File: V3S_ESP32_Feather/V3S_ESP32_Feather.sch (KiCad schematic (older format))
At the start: 10 parts, among them J1 USB_B_Micro, J10 UART, J2 Bat, J4 PWM, J8 I2C

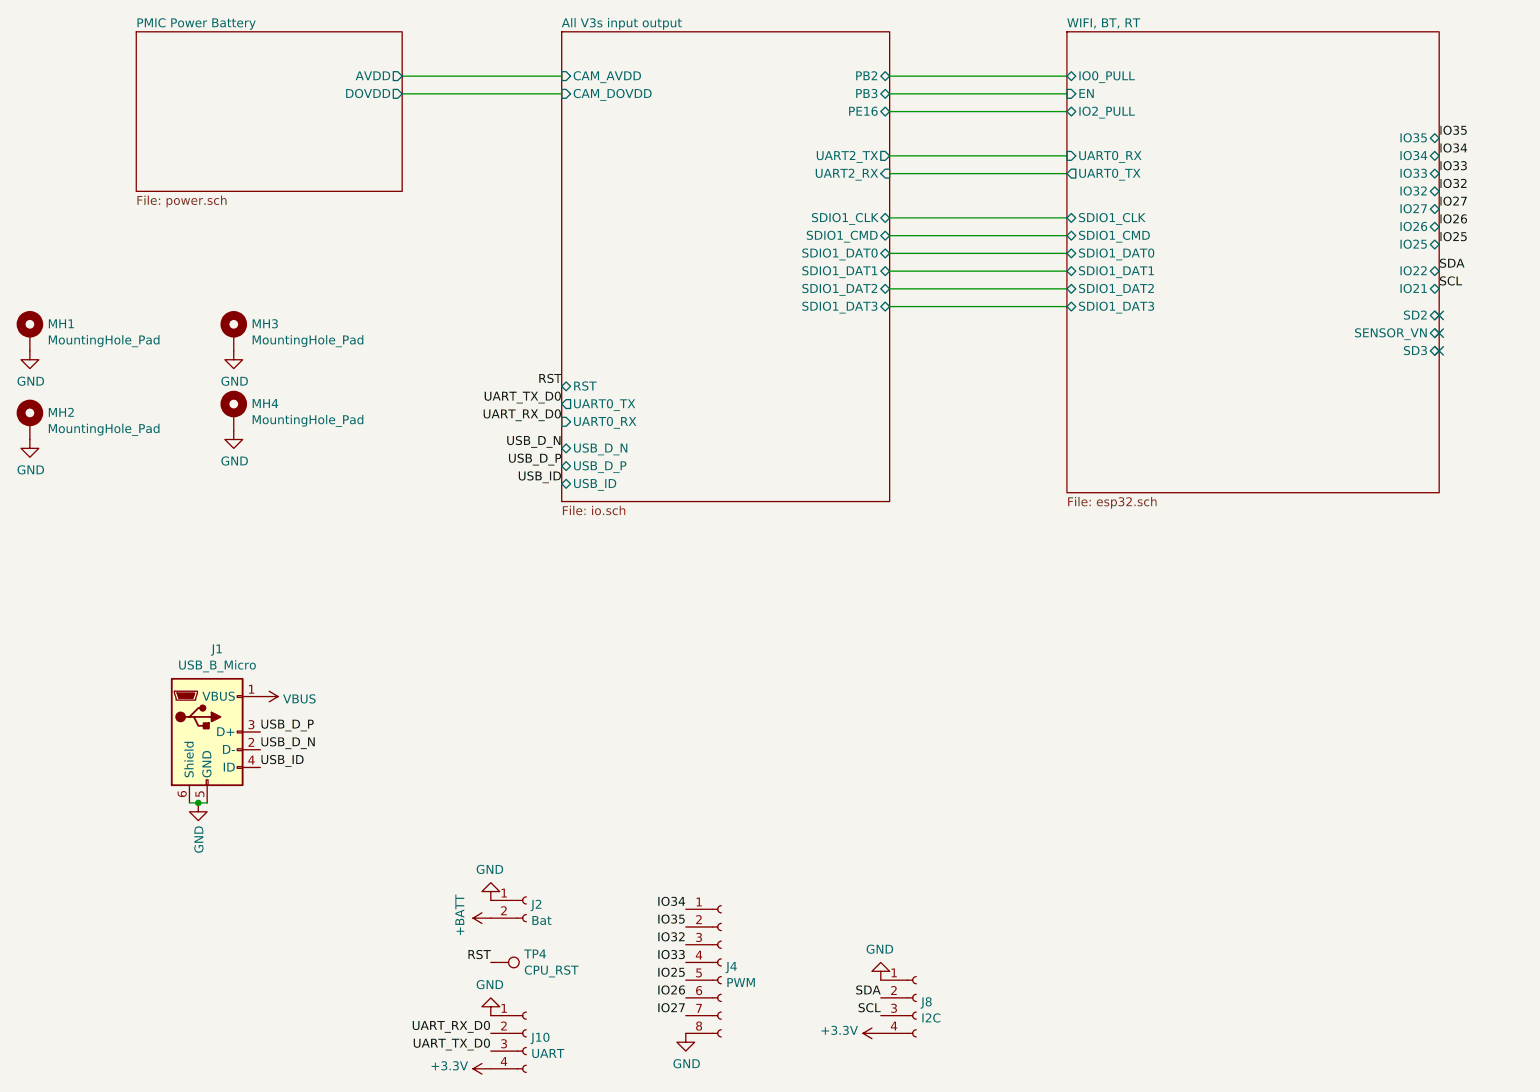
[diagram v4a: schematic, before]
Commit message: Sdcard part routed
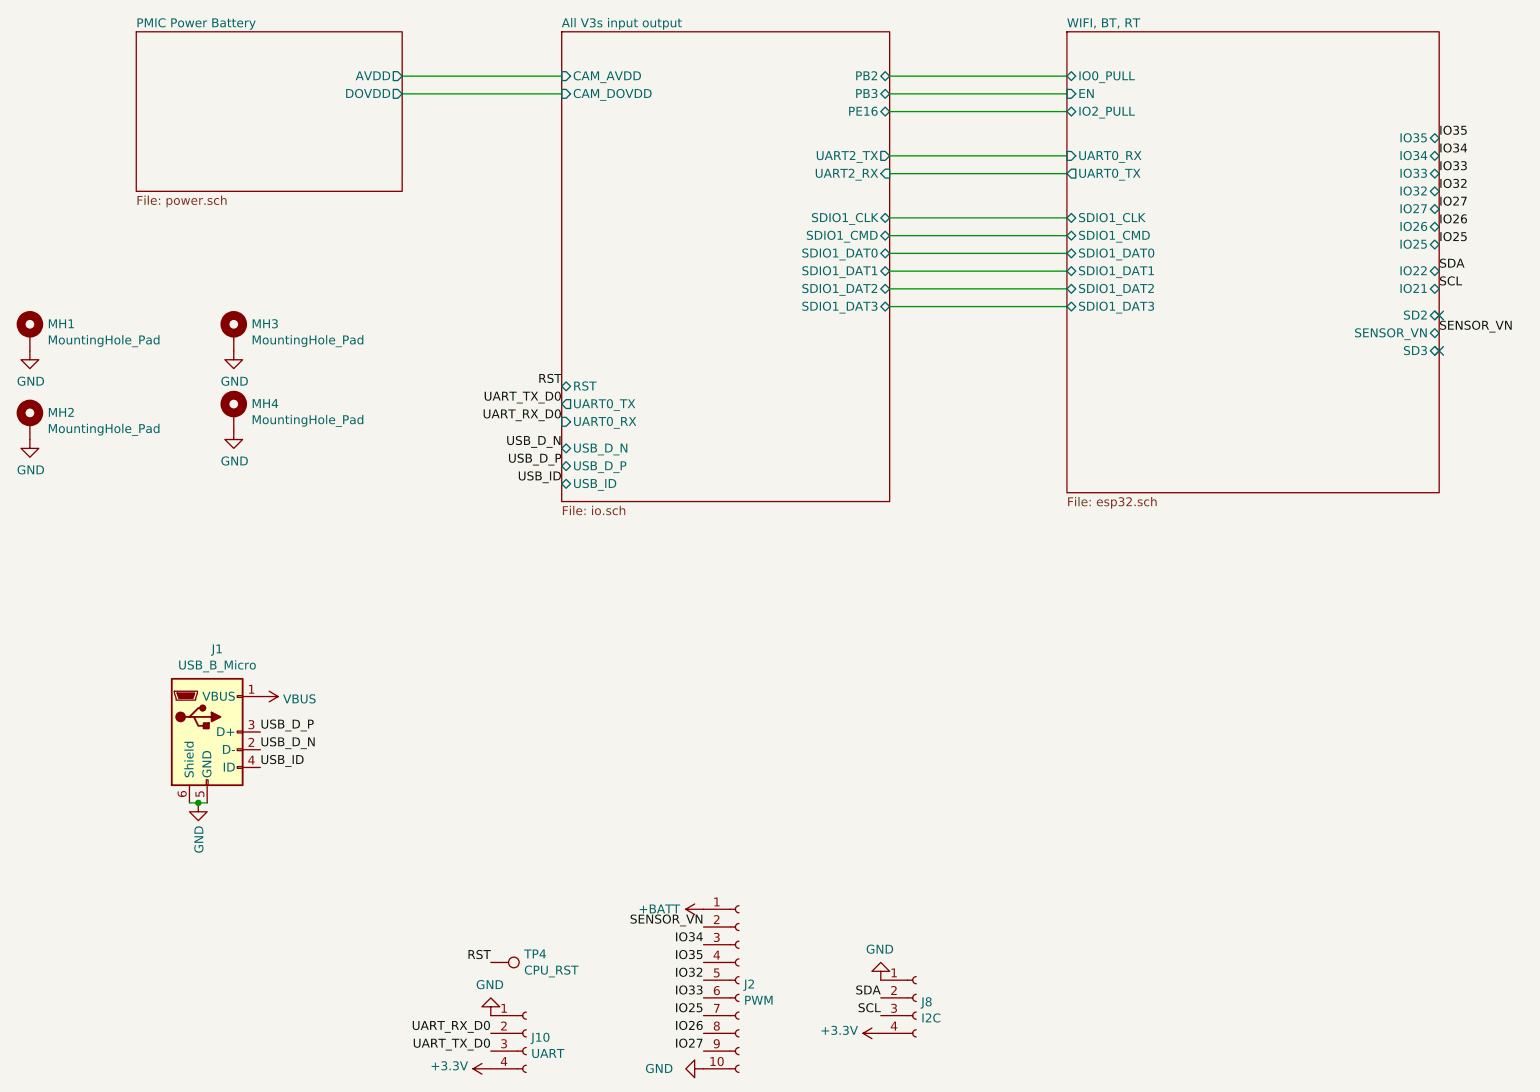
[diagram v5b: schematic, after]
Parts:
- removed J2: Bat, Connector_JST:JST_SH_SM02B-SRSS-TB_1x02-1MP_P1.00mm_Horizontal, symbol Connector:Conn_01x02_Female
- removed J4: PWM, Connector_JST:JST_SH_SM08B-SRSS-TB_1x08-1MP_P1.00mm_Horizontal, symbol Connector:Conn_01x08_Female
- added J2: PWM, Connector_JST:JST_SH_SM10B-SRSS-TB_1x10-1MP_P1.00mm_Horizontal, symbol Connector:Conn_01x10_Female
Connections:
- net +BATT: now also J2.1 (Pin_1)
- net GND: now also J2.10 (Pin_10)
- net IO25: now also J2.7 (Pin_7)
- net IO26: now also J2.8 (Pin_8)
- net IO27: now also J2.9 (Pin_9)
- net IO32: now also J2.5 (Pin_5)
- net IO33: now also J2.6 (Pin_6)
- net IO34: now also J2.3 (Pin_3)
- net IO35: now also J2.4 (Pin_4)
- new net SENSOR_VN: J2.2 (Pin_2)
- no-connect marks 3 -> 2
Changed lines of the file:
@@
 Text Label 3650 3750 2    50   ~ 0
 USB_D_P
-$Comp
-L Connector:Conn_01x08_Female J4
-U 1 1 5D7F05A5
-P 4550 6550
-F 0 "J4" H 4578 6526 50  0000 L CNN
-F 1 "PWM" H 4578 6435 50  0000 L CNN
-F 2 "Connector_JST:JST_SH_SM08B-SRSS-TB_1x08-1MP_P1.00mm_Horizontal" H 4550 6550 50  0001 C CNN
-F 3 "~" H 4550 6550 50  0001 C CNN
-	1    4550 6550
-	1    0    0    -1
-$EndComp
-$Comp
-L Connector:Conn_01x02_Female J2
-U 1 1 5D7FE5F6
-P 3450 6200
-F 0 "J2" H 3478 6176 50  0000 L CNN
-F 1 "Bat" H 3478 6085 50  0000 L CNN
-F 2 "Connector_JST:JST_SH_SM02B-SRSS-TB_1x02-1MP_P1.00mm_Horizontal" H 3450 6200 50  0001 C CNN
-F 3 "~" H 3450 6200 50  0001 C CNN
-	1    3450 6200
-	1    0    0    -1
-$EndComp
 Text Label 8600 2100 0    50   ~ 0
 IO33
@@
 Text Label 8600 2500 0    50   ~ 0
 IO25
-Text Label 4350 6550 2    50   ~ 0
+Text Label 4450 6750 2    50   ~ 0
 IO33
-Text Label 4350 6450 2    50   ~ 0
+Text Label 4450 6650 2    50   ~ 0
 IO32
-Text Label 4350 6850 2    50   ~ 0
+Text Label 4450 7050 2    50   ~ 0
 IO27
-Text Label 4350 6750 2    50   ~ 0
+Text Label 4450 6950 2    50   ~ 0
 IO26
-Text Label 4350 6650 2    50   ~ 0
+Text Label 4450 6850 2    50   ~ 0
 IO25
 $Comp
 L power:GND #PWR0125
 U 1 1 5D81A9F6
-P 4350 6950
-F 0 "#PWR0125" H 4350 6700 50  0001 C CNN
-F 1 "GND" H 4355 6777 50  0000 C CNN
-F 2 "" H 4350 6950 50  0001 C CNN
-F 3 "" H 4350 6950 50  0001 C CNN
-	1    4350 6950
-	1    0    0    -1
+P 4450 7150
+F 0 "#PWR0125" H 4450 6900 50  0001 C CNN
+F 1 "GND" V 4450 6900 50  0000 C CNN
+F 2 "" H 4450 7150 50  0001 C CNN
+F 3 "" H 4450 7150 50  0001 C CNN
+	1    4450 7150
+	0    1    1    0
 $EndComp
 Text Label 8600 2000 0    50   ~ 0
 IO34
-Text Label 4350 6250 2    50   ~ 0
+Text Label 4450 6450 2    50   ~ 0
 IO34
 Text Label 8600 2650 0    50   ~ 0
@@
 L power:+BATT #PWR?
 U 1 1 5D8514B2
-P 3250 6300
+P 4450 6250
 AR Path="/5BC231CB/5D8514B2" Ref="#PWR?"  Part="1"
 AR Path="/5D8514B2" Ref="#PWR0144"  Part="1"
-F 0 "#PWR0144" H 3250 6150 50  0001 C CNN
-F 1 "+BATT" H 3265 6473 50  0000 C CNN
-F 2 "" H 3250 6300 50  0001 C CNN
-F 3 "" H 3250 6300 50  0001 C CNN
-	1    3250 6300
+F 0 "#PWR0144" H 4450 6100 50  0001 C CNN
+F 1 "+BATT" V 4450 6500 50  0000 C CNN
+F 2 "" H 4450 6250 50  0001 C CNN
+F 3 "" H 4450 6250 50  0001 C CNN
+	1    4450 6250
 	0    -1   -1   0
-$EndComp
-$Comp
-L power:GND #PWR0147
-U 1 1 5D8522F8
-P 3250 6200
-F 0 "#PWR0147" H 3250 5950 50  0001 C CNN
-F 1 "GND" H 3255 6027 50  0000 C CNN
-F 2 "" H 3250 6200 50  0001 C CNN
-F 3 "" H 3250 6200 50  0001 C CNN
-	1    3250 6200
-	-1   0    0    1
 $EndComp
 $Comp
@@
 $EndSheet
 NoConn ~ 8600 3100
-Text Label 4350 6350 2    50   ~ 0
+Text Label 4450 6550 2    50   ~ 0
 IO35
 Text Label 8600 1900 0    50   ~ 0
@@
 $EndComp
 NoConn ~ 8600 2900
-NoConn ~ 8600 3000
+$Comp
+L Connector:Conn_01x10_Female J2
+U 1 1 5D909E64
+P 4650 6650
+F 0 "J2" H 4678 6626 50  0000 L CNN
+F 1 "PWM" H 4678 6535 50  0000 L CNN
+F 2 "Connector_JST:JST_SH_SM10B-SRSS-TB_1x10-1MP_P1.00mm_Horizontal" H 4650 6650 50  0001 C CNN
+F 3 "~" H 4650 6650 50  0001 C CNN
+	1    4650 6650
+	1    0    0    -1
+$EndComp
+Text Label 8600 3000 0    50   ~ 0
+SENSOR_VN
+Text Label 4450 6350 2    50   ~ 0
+SENSOR_VN
 $EndSCHEMATC

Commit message: last 4 layers version
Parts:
- removed J2: PWM, Connector_JST:JST_SH_SM10B-SRSS-TB_1x10-1MP_P1.00mm_Horizontal, symbol Connector:Conn_01x10_Female
- removed J8: I2C, Connector_JST:JST_SH_SM04B-SRSS-TB_1x04-1MP_P1.00mm_Horizontal, symbol Connector:Conn_01x04_Female
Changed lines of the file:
@@
 Text Label 3650 3750 2    50   ~ 0
 USB_D_P
-Text Label 8600 2100 0    50   ~ 0
-IO33
-Text Label 8600 2200 0    50   ~ 0
-IO32
-Text Label 8600 2300 0    50   ~ 0
-IO27
-Text Label 8600 2400 0    50   ~ 0
-IO26
-Text Label 8600 2500 0    50   ~ 0
-IO25
-Text Label 4450 6750 2    50   ~ 0
-IO33
-Text Label 4450 6650 2    50   ~ 0
-IO32
-Text Label 4450 7050 2    50   ~ 0
-IO27
-Text Label 4450 6950 2    50   ~ 0
-IO26
-Text Label 4450 6850 2    50   ~ 0
-IO25
-$Comp
-L power:GND #PWR0125
-U 1 1 5D81A9F6
-P 4450 7150
-F 0 "#PWR0125" H 4450 6900 50  0001 C CNN
-F 1 "GND" V 4450 6900 50  0000 C CNN
-F 2 "" H 4450 7150 50  0001 C CNN
-F 3 "" H 4450 7150 50  0001 C CNN
-	1    4450 7150
-	0    1    1    0
-$EndComp
-Text Label 8600 2000 0    50   ~ 0
-IO34
-Text Label 4450 6450 2    50   ~ 0
-IO34
-Text Label 8600 2650 0    50   ~ 0
-SDA
-Text Label 8600 2750 0    50   ~ 0
-SCL
-Text Label 5450 6750 2    50   ~ 0
-SDA
-Text Label 5450 6850 2    50   ~ 0
-SCL
-$Comp
-L Connector:Conn_01x04_Female J8
-U 1 1 5D82F81A
-P 5650 6750
-F 0 "J8" H 5678 6726 50  0000 L CNN
-F 1 "I2C" H 5678 6635 50  0000 L CNN
-F 2 "Connector_JST:JST_SH_SM04B-SRSS-TB_1x04-1MP_P1.00mm_Horizontal" H 5650 6750 50  0001 C CNN
-F 3 "~" H 5650 6750 50  0001 C CNN
-	1    5650 6750
-	1    0    0    -1
-$EndComp
-$Comp
-L power:GND #PWR0130
-U 1 1 5D82F822
-P 5450 6650
-F 0 "#PWR0130" H 5450 6400 50  0001 C CNN
-F 1 "GND" H 5455 6477 50  0000 C CNN
-F 2 "" H 5450 6650 50  0001 C CNN
-F 3 "" H 5450 6650 50  0001 C CNN
-	1    5450 6650
-	-1   0    0    1
-$EndComp
-$Comp
-L power:+3.3V #PWR0132
-U 1 1 5D82F828
-P 5450 6950
-F 0 "#PWR0132" H 5450 6800 50  0001 C CNN
-F 1 "+3.3V" V 5465 7078 50  0000 L CNN
-F 2 "" H 5450 6950 50  0001 C CNN
-F 3 "" H 5450 6950 50  0001 C CNN
-	1    5450 6950
-	0    -1   -1   0
-$EndComp
 $Comp
 L power:GND #PWR0135
@@
 	1    1950 5050
 	0    1    1    0
-$EndComp
-$Comp
-L power:+BATT #PWR?
-U 1 1 5D8514B2
-P 4450 6250
-AR Path="/5BC231CB/5D8514B2" Ref="#PWR?"  Part="1"
-AR Path="/5D8514B2" Ref="#PWR0144"  Part="1"
-F 0 "#PWR0144" H 4450 6100 50  0001 C CNN
-F 1 "+BATT" V 4450 6500 50  0000 C CNN
-F 2 "" H 4450 6250 50  0001 C CNN
-F 3 "" H 4450 6250 50  0001 C CNN
-	1    4450 6250
-	0    -1   -1   0
 $EndComp
 $Comp
@@
 F11 "SDIO1_DAT0" B L 6500 2550 50
 F12 "IO0_PULL" B L 6500 1550 50
-F13 "IO35" B R 8600 1900 50
-F14 "IO34" B R 8600 2000 50
-F15 "IO33" B R 8600 2100 50
-F16 "IO32" B R 8600 2200 50
-F17 "IO27" B R 8600 2300 50
-F18 "IO26" B R 8600 2400 50
-F19 "IO25" B R 8600 2500 50
-F20 "IO22" B R 8600 2650 50
-F21 "IO21" B R 8600 2750 50
-F22 "SENSOR_VN" B R 8600 3000 50
-F23 "SD2" B R 8600 2900 50
-F24 "SD3" B R 8600 3100 50
+F13 "SD2" B R 8600 2900 50
+F14 "SD3" B R 8600 3100 50
 $EndSheet
 NoConn ~ 8600 3100
-Text Label 4450 6550 2    50   ~ 0
-IO35
-Text Label 8600 1900 0    50   ~ 0
-IO35
 Text Label 3250 6950 2    50   ~ 0
 UART_RX_D0
@@
 $EndComp
 NoConn ~ 8600 2900
-$Comp
-L Connector:Conn_01x10_Female J2
-U 1 1 5D909E64
-P 4650 6650
-F 0 "J2" H 4678 6626 50  0000 L CNN
-F 1 "PWM" H 4678 6535 50  0000 L CNN
-F 2 "Connector_JST:JST_SH_SM10B-SRSS-TB_1x10-1MP_P1.00mm_Horizontal" H 4650 6650 50  0001 C CNN
-F 3 "~" H 4650 6650 50  0001 C CNN
-	1    4650 6650
-	1    0    0    -1
-$EndComp
-Text Label 8600 3000 0    50   ~ 0
-SENSOR_VN
-Text Label 4450 6350 2    50   ~ 0
-SENSOR_VN
 $EndSCHEMATC

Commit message: Power part autorouted, replaced micro usb connector by jst sh 5 pin
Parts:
- J1: footprint Connector_USB:USB_Micro-B_Molex-105017-0001 -> Connector_JST:JST_SH_BM05B-SRSS-TB_1x05-1MP_P1.00mm_Vertical
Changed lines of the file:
@@
 F 0 "J1" H 1707 5717 50  0000 C CNN
 F 1 "USB_B_Micro" H 1707 5626 50  0000 C CNN
-F 2 "Connector_USB:USB_Micro-B_Molex-105017-0001" H 1800 5200 50  0001 C CNN
+F 2 "Connector_JST:JST_SH_BM05B-SRSS-TB_1x05-1MP_P1.00mm_Vertical" H 1800 5200 50  0001 C CNN
 F 3 "~" H 1800 5200 50  0001 C CNN
 	1    1650 5250

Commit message: progress on pcb cleaning
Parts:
- removed J1: USB_B_Micro, Connector_JST:JST_SH_BM05B-SRSS-TB_1x05-1MP_P1.00mm_Vertical, symbol Connector:USB_B_Micro
- added J1: USB_Micro, Connector_JST:JST_SH_BM05B-SRSS-TB_1x05-1MP_P1.00mm_Vertical, symbol Connector:Conn_01x05_Female
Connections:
- net GND: now also J1.1 (Pin_1)
- net USB_D_N: now also J1.3 (Pin_3)
- net USB_D_P: now also J1.2 (Pin_2)
- net USB_ID: now also J1.5 (Pin_5)
- net VBUS: now also J1.4 (Pin_4)
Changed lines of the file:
@@
 Text Label 3650 3500 2    50   ~ 0
 UART_RX_D0
-Text Label 1950 5350 0    50   ~ 0
+Text Label 2050 4450 2    50   ~ 0
 USB_D_N
-Text Label 1950 5250 0    50   ~ 0
+Text Label 2050 4350 2    50   ~ 0
 USB_D_P
 Text Label 3650 3650 2    50   ~ 0
@@
 L power:GND #PWR0135
 U 1 1 5D83F449
-P 1600 5650
-F 0 "#PWR0135" H 1600 5400 50  0001 C CNN
-F 1 "GND" V 1605 5522 50  0000 R CNN
-F 2 "" H 1600 5650 50  0001 C CNN
-F 3 "" H 1600 5650 50  0001 C CNN
-	1    1600 5650
-	1    0    0    -1
+P 2050 4250
+F 0 "#PWR0135" H 2050 4000 50  0001 C CNN
+F 1 "GND" V 2055 4122 50  0000 R CNN
+F 2 "" H 2050 4250 50  0001 C CNN
+F 3 "" H 2050 4250 50  0001 C CNN
+	1    2050 4250
+	0    1    1    0
 $EndComp
 Text Label 3650 3300 2    50   ~ 0
@@
 L power:VBUS #PWR0143
 U 1 1 5D84C767
-P 1950 5050
-F 0 "#PWR0143" H 1950 4900 50  0001 C CNN
-F 1 "VBUS" V 1965 5178 50  0000 L CNN
-F 2 "" H 1950 5050 50  0001 C CNN
-F 3 "" H 1950 5050 50  0001 C CNN
-	1    1950 5050
-	0    1    1    0
+P 2050 4550
+F 0 "#PWR0143" H 2050 4400 50  0001 C CNN
+F 1 "VBUS" V 2065 4678 50  0000 L CNN
+F 2 "" H 2050 4550 50  0001 C CNN
+F 3 "" H 2050 4550 50  0001 C CNN
+	1    2050 4550
+	0    -1   -1   0
 $EndComp
 $Comp
@@
 	0    1    1    0
 $EndComp
-$Comp
-L Connector:USB_B_Micro J1
-U 1 1 5D8C9C3C
-P 1650 5250
-F 0 "J1" H 1707 5717 50  0000 C CNN
-F 1 "USB_B_Micro" H 1707 5626 50  0000 C CNN
-F 2 "Connector_JST:JST_SH_BM05B-SRSS-TB_1x05-1MP_P1.00mm_Vertical" H 1800 5200 50  0001 C CNN
-F 3 "~" H 1800 5200 50  0001 C CNN
-	1    1650 5250
-	1    0    0    -1
-$EndComp
-Wire Wire Line
-	1550 5650 1600 5650
-Connection ~ 1600 5650
-Wire Wire Line
-	1600 5650 1650 5650
 Text Label 3650 3850 2    50   ~ 0
 USB_ID
-Text Label 1950 5450 0    50   ~ 0
+Text Label 2050 4650 2    50   ~ 0
 USB_ID
 $Sheet
@@
 $EndComp
 NoConn ~ 8600 2900
+$Comp
+L Connector:Conn_01x05_Female J1
+U 1 1 5DB4220C
+P 2250 4450
+F 0 "J1" H 2278 4476 50  0000 L CNN
+F 1 "USB_Micro" H 2278 4385 50  0000 L CNN
+F 2 "Connector_JST:JST_SH_BM05B-SRSS-TB_1x05-1MP_P1.00mm_Vertical" H 2250 4450 50  0001 C CNN
+F 3 "~" H 2250 4450 50  0001 C CNN
+	1    2250 4450
+	1    0    0    -1
+$EndComp
 $EndSCHEMATC
